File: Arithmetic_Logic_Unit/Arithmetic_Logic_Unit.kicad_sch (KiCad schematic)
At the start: 0 parts

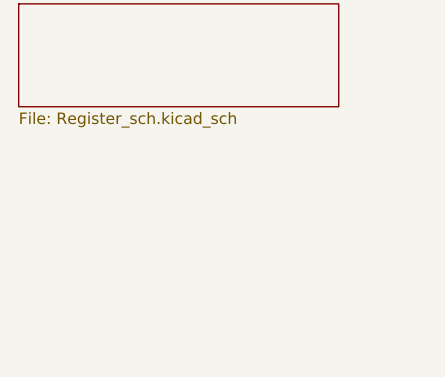
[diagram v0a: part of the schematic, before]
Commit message: added A, B, and Instructional Regsiters
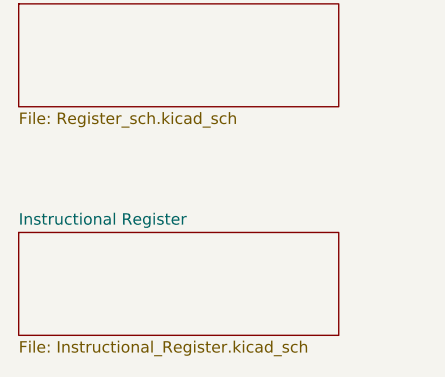
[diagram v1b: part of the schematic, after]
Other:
- added sheet Instructional Register (Instructional_Register.kicad_sch)
- company: (none) -> Arsenal Gear
- title: (none) -> Arithmethic Logic Unit
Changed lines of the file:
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@@
 	(generator_version "8.0")
 	(paper "A4")
+	(title_block
+		(title "Arithmethic Logic Unit")
+		(date "2024-11-11")
+		(company "Arsenal Gear")
+	)
+	(sheet
+		(at 39.37 50.8)
+		(size 35.56 11.43)
+		(fields_autoplaced yes)
+		(stroke
+			(width 0.1524)
+			(type solid)
+		)
+		(fill
+			(color 0 0 0 0.0000)
+		)
+		(property "Sheetname" "Instructional Register"
+			(at 39.37 50.0884 0)
+			(effects
+				(font
+					(size 1.27 1.27)
+				)
+				(justify left bottom)
+			)
+		)
+		(property "Sheetfile" "Instructional_Register.kicad_sch"
+			(at 39.37 62.8146 0)
+			(effects
+				(font
+					(size 1.27 1.27)
+				)
+				(justify left top)
+			)
+		)
+		(instances
+			(project "Arithmetic_Logic_Unit"
+				(path "/71235e3f-9de8-4596-887a-1aa4526e80d1"
+					(page "3")
+				)
+			)
+		)
+	)
 	(sheet
 		(at 39.37 25.4)

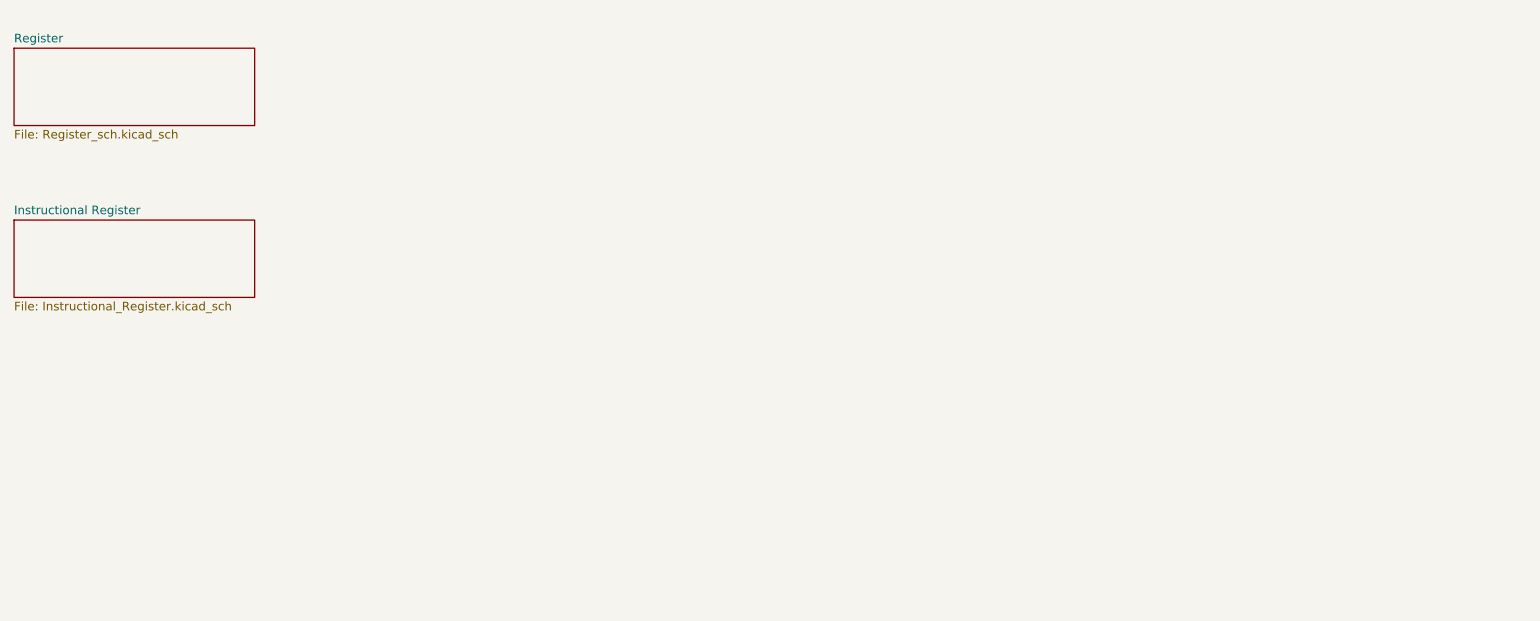
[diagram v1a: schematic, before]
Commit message: updated wiki, created board outline for alu, made registers with hierarchical label
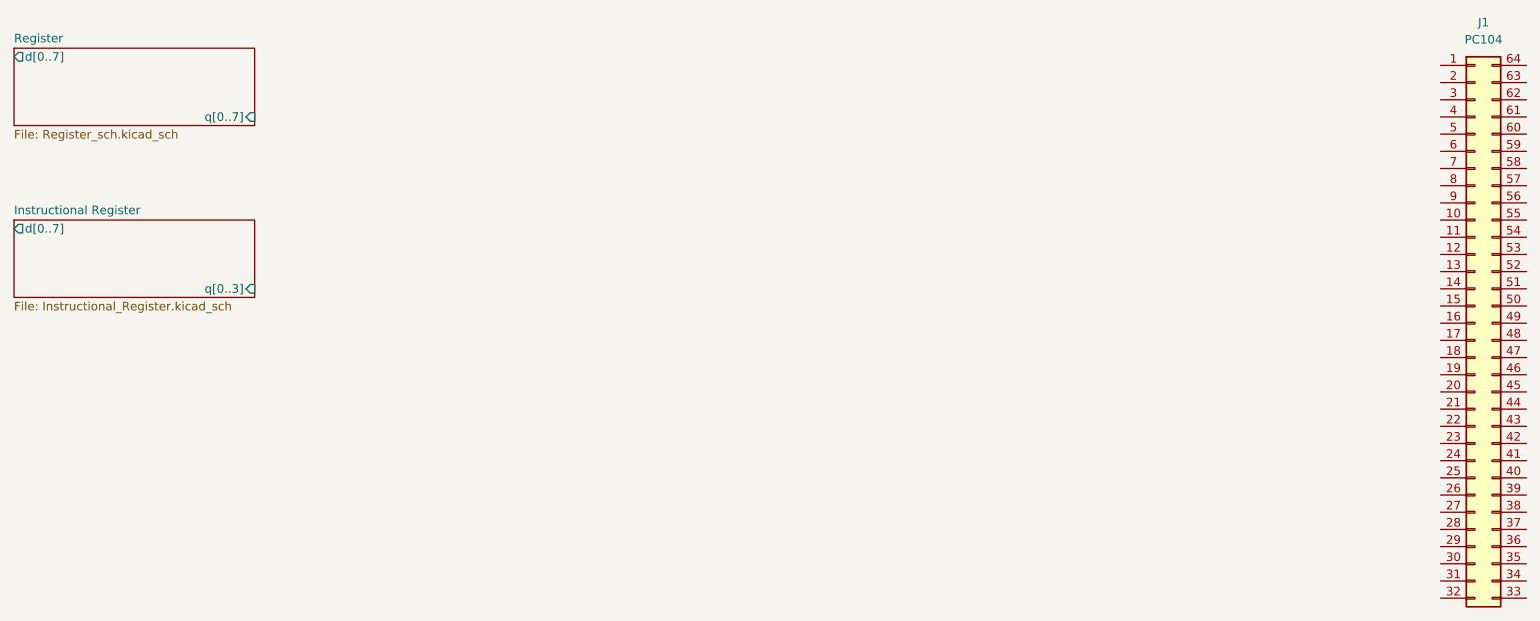
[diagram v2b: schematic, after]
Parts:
- added J1: PC104, Connector_PinSocket_2.54mm:PinSocket_2x32_P2.54mm_Vertical, symbol Connector_Generic:Conn_02x32_Counter_Clockwise
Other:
- sheet Instructional Register ports: added d[0..7], q[0..3]; removed none
- sheet Register ports: added d[0..7], q[0..7]; removed none
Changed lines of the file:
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@@
 		(company "Arsenal Gear")
+	)
+	(symbol
+		(lib_id "Connector_Generic:Conn_02x32_Counter_Clockwise")
+		(at 255.27 66.04 0)
+		(unit 1)
+		(exclude_from_sim no)
+		(in_bom yes)
+		(on_board yes)
+		(dnp no)
+		(fields_autoplaced yes)
+		(property "Reference" "J1"
+			(at 256.54 21.59 0)
+			(effects
+				(font
+					(size 1.27 1.27)
+				)
+			)
+		)
+		(property "Value" "PC104"
+			(at 256.54 24.13 0)
+			(effects
+				(font
+					(size 1.27 1.27)
+				)
+			)
+		)
+		(property "Footprint" "Connector_PinSocket_2.54mm:PinSocket_2x32_P2.54mm_Vertical"
+			(at 255.27 66.04 0)
+			(effects
+				(font
+					(size 1.27 1.27)
+				)
+				(hide yes)
+			)
+		)
+		(property "Datasheet" "~"
+			(at 255.27 66.04 0)
+			(effects
+				(font
+					(size 1.27 1.27)
+				)
+				(hide yes)
+			)
+		)
+		(property "Description" "Generic connector, double row, 02x32, counter clockwise pin numbering scheme (similar to DIP package numbering), script generated (kicad-library-utils/schlib/autogen/connector/)"
+			(at 255.27 66.04 0)
+			(effects
+				(font
+					(size 1.27 1.27)
+				)
+				(hide yes)
+			)
+		)
+		(pin "26"
+		)
+		(pin "9"
+		)
+		(pin "57"
+		)
+		(pin "31"
+		)
+		(pin "16"
+		)
+		(pin "2"
+		)
+		(pin "23"
+		)
+		(pin "42"
+		)
+		(pin "7"
+		)
+		(pin "39"
+		)
+		(pin "48"
+		)
+		(pin "5"
+		)
+		(pin "47"
+		)
+		(pin "43"
+		)
+		(pin "52"
+		)
+		(pin "62"
+		)
+		(pin "24"
+		)
+		(pin "44"
+		)
+		(pin "59"
+		)
+		(pin "8"
+		)
+		(pin "37"
+		)
+		(pin "4"
+		)
+		(pin "27"
+		)
+		(pin "6"
+		)
+		(pin "61"
+		)
+		(pin "22"
+		)
+		(pin "20"
+		)
+		(pin "41"
+		)
+		(pin "32"
+		)
+		(pin "45"
+		)
+		(pin "21"
+		)
+		(pin "50"
+		)
+		(pin "30"
+		)
+		(pin "58"
+		)
+		(pin "46"
+		)
+		(pin "64"
+		)
+		(pin "25"
+		)
+		(pin "34"
+		)
+		(pin "18"
+		)
+		(pin "40"
+		)
+		(pin "38"
+		)
+		(pin "36"
+		)
+		(pin "28"
+		)
+		(pin "14"
+		)
+		(pin "13"
+		)
+		(pin "12"
+		)
+		(pin "60"
+		)
+		(pin "35"
+		)
+		(pin "56"
+		)
+		(pin "63"
+		)
+		(pin "10"
+		)
+		(pin "11"
+		)
+		(pin "1"
+		)
+		(pin "33"
+		)
+		(pin "15"
+		)
+		(pin "3"
+		)
+		(pin "19"
+		)
+		(pin "54"
+		)
+		(pin "49"
+		)
+		(pin "55"
+		)
+		(pin "29"
+		)
+		(pin "53"
+		)
+		(pin "51"
+		)
+		(pin "17"
+		)
+		(instances
+			(project "Arithmetic_Logic_Unit"
+				(path "/71235e3f-9de8-4596-887a-1aa4526e80d1"
+					(reference "J1")
+					(unit 1)
+				)
+			)
+		)
 	)
 	(sheet
@@
 			)
 		)
+		(pin "q[0..3]" input
+			(at 74.93 60.96 0)
+			(effects
+				(font
+					(size 1.27 1.27)
+				)
+				(justify right)
+			)
+		)
+		(pin "d[0..7]" output
+			(at 39.37 52.07 180)
+			(effects
+				(font
+					(size 1.27 1.27)
+				)
+				(justify left)
+			)
+		)
 		(instances
 			(project "Arithmetic_Logic_Unit"
@@
 			)
 		)
+		(pin "q[0..7]" input
+			(at 74.93 35.56 0)
+			(effects
+				(font
+					(size 1.27 1.27)
+				)
+				(justify right)
+			)
+		)
+		(pin "d[0..7]" output
+			(at 39.37 26.67 180)
+			(effects
+				(font
+					(size 1.27 1.27)
+				)
+				(justify left)
+			)
+		)

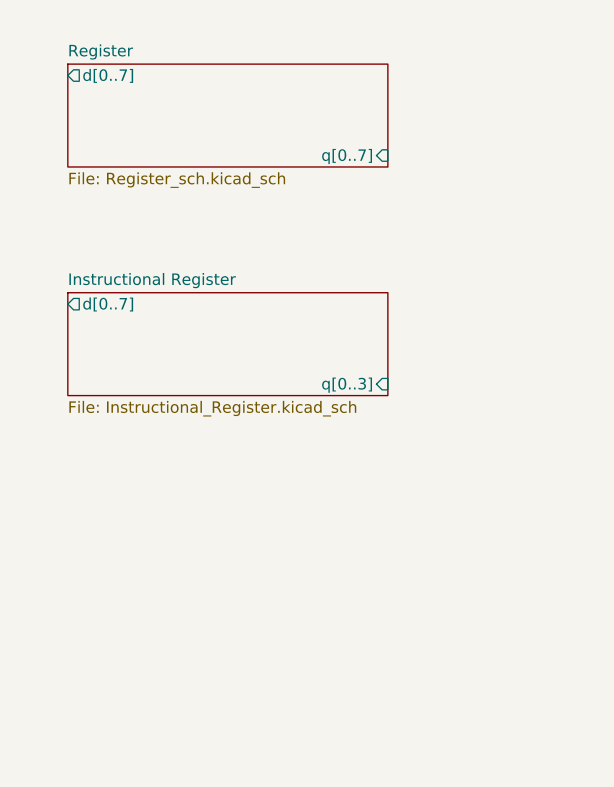
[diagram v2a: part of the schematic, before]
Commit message: fixed register schematic
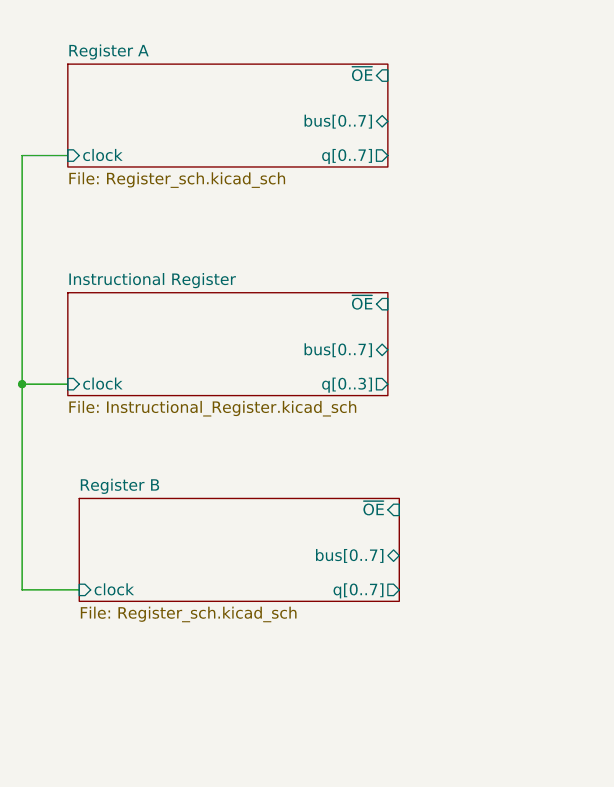
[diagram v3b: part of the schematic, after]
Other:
- sheet Register renamed Register A
- added sheet Register B (Register_sch.kicad_sch)
- sheet Instructional Register ports: added bus[0..7], clock, ~{OE}; removed d[0..7]
- sheet Register A ports: added bus[0..7], clock, ~{OE}; removed d[0..7]
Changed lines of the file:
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@@
 		(company "Arsenal Gear")
+	)
+	(junction
+		(at 34.29 60.96)
+		(diameter 0)
+		(color 0 0 0 0)
+	)
+	(wire
+		(pts
+			(xy 34.29 60.96) (xy 39.37 60.96)
+		)
+		(stroke
+			(width 0)
+			(type default)
+		)
+	)
+	(wire
+		(pts
+			(xy 39.37 35.56) (xy 34.29 35.56)
+		)
+		(stroke
+			(width 0)
+			(type default)
+		)
+	)
+	(wire
+		(pts
+			(xy 34.29 60.96) (xy 34.29 83.82)
+		)
+		(stroke
+			(width 0)
+			(type default)
+		)
+	)
+	(wire
+		(pts
+			(xy 34.29 83.82) (xy 40.64 83.82)
+		)
+		(stroke
+			(width 0)
+			(type default)
+		)
+	)
+	(wire
+		(pts
+			(xy 34.29 35.56) (xy 34.29 60.96)
+		)
+		(stroke
+			(width 0)
+			(type default)
+		)
 	)
 	(symbol
@@
 			)
 		)
-		(pin "q[0..3]" input
+		(pin "clock" input
+			(at 39.37 60.96 180)
+			(effects
+				(font
+					(size 1.27 1.27)
+				)
+				(justify left)
+			)
+		)
+		(pin "~{OE}" input
+			(at 74.93 52.07 0)
+			(effects
+				(font
+					(size 1.27 1.27)
+				)
+				(justify right)
+			)
+		)
+		(pin "bus[0..7]" bidirectional
+			(at 74.93 57.15 0)
+			(effects
+				(font
+					(size 1.27 1.27)
+				)
+				(justify right)
+			)
+		)
+		(pin "q[0..3]" output
 			(at 74.93 60.96 0)
 			(effects
@@
 				)
 				(justify right)
-			)
-		)
-		(pin "d[0..7]" output
-			(at 39.37 52.07 180)
-			(effects
-				(font
-					(size 1.27 1.27)
-				)
-				(justify left)
 			)
 		)
@@
 			(color 0 0 0 0.0000)
 		)
-		(property "Sheetname" "Register"
+		(property "Sheetname" "Register A"
 			(at 39.37 24.6884 0)
 			(effects
@@
 			)
 		)
-		(pin "q[0..7]" input
+		(pin "clock" input
+			(at 39.37 35.56 180)
+			(effects
+				(font
+					(size 1.27 1.27)
+				)
+				(justify left)
+			)
+		)
+		(pin "~{OE}" input
+			(at 74.93 26.67 0)
+			(effects
+				(font
+					(size 1.27 1.27)
+				)
+				(justify right)
+			)
+		)
+		(pin "q[0..7]" output
 			(at 74.93 35.56 0)
 			(effects
@@
 			)
 		)
-		(pin "d[0..7]" output
-			(at 39.37 26.67 180)
-			(effects
-				(font
-					(size 1.27 1.27)
-				)
-				(justify left)
+		(pin "bus[0..7]" bidirectional
+			(at 74.93 31.75 0)
+			(effects
+				(font
+					(size 1.27 1.27)
+				)
+				(justify right)
 			)
 		)
@@
 				)
 			)
+		)
+	)
+	(sheet
+		(at 40.64 73.66)
+		(size 35.56 11.43)
+		(fields_autoplaced yes)
+		(stroke
+			(width 0.1524)
+			(type solid)
+		)
+		(fill
+			(color 0 0 0 0.0000)
+		)
+		(property "Sheetname" "Register B"
+			(at 40.64 72.9484 0)
+			(effects
+				(font
+					(size 1.27 1.27)
+				)
+				(justify left bottom)
+			)
+		)
+		(property "Sheetfile" "Register_sch.kicad_sch"
+			(at 40.64 85.6746 0)
+			(effects
+				(font
+					(size 1.27 1.27)
+				)
+				(justify left top)
+			)
+		)
+		(pin "clock" input
+			(at 40.64 83.82 180)
+			(effects
+				(font
+					(size 1.27 1.27)
+				)
+				(justify left)
+			)
+		)
+		(pin "~{OE}" input
+			(at 76.2 74.93 0)
+			(effects
+				(font
+					(size 1.27 1.27)
+				)
+				(justify right)
+			)
+		)
+		(pin "q[0..7]" output
+			(at 76.2 83.82 0)
+			(effects
+				(font
+					(size 1.27 1.27)
+				)
+				(justify right)
+			)
+		)
+		(pin "bus[0..7]" bidirectional
+			(at 76.2 80.01 0)
+			(effects
+				(font
+					(size 1.27 1.27)
+				)
+				(justify right)
+			)
+		)
+		(instances
+			(project "Arithmetic_Logic_Unit"
+				(path "/71235e3f-9de8-4596-887a-1aa4526e80d1"
+					(page "4")
+				)
+			)
